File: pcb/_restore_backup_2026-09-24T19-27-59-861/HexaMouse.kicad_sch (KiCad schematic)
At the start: 23 parts, among them J1 Conn_01x02_Socket, J2 Conn_01x02_Socket, J3 Xiao_Headers_Left, J4 Xiao_Headers_Right, SW1 SW_SPDT, U2 TLV493D, U3 TLV493D, U4 TLV493D, U5 TCA9548APWR

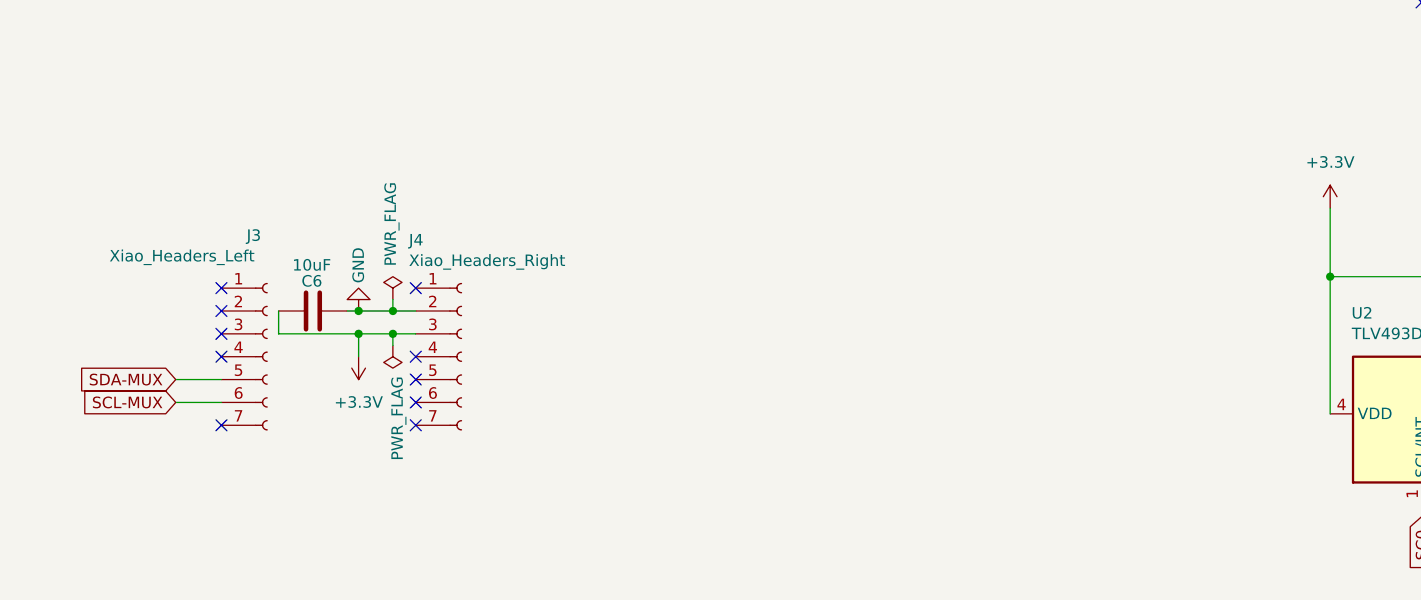
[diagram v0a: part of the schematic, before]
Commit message: Swapped from MCU to pins so i can use headers instead
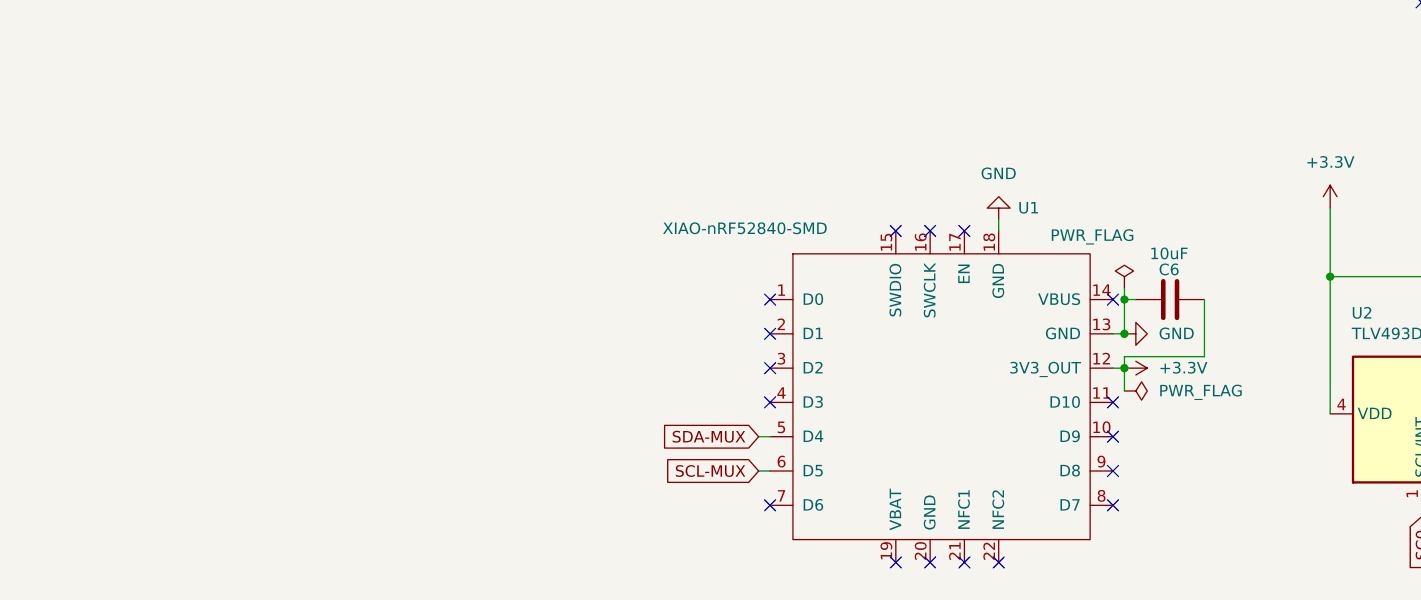
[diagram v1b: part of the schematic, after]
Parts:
- removed J3: Xiao_Headers_Left, symbol Connector:Conn_01x07_Socket
- removed J4: Xiao_Headers_Right, symbol Connector:Conn_01x07_Socket
- added U1: XIAO-nRF52840-SMD, Seeed_Studio_XIAO_Series:XIAO-nRF52840-SMD, symbol Seeed_Studio_XIAO_Series:XIAO-nRF52840-SMD
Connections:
- net +3.3V: now also C6.1, U1.12 (3V3_OUT); no longer C6.2
- net GND: now also C6.2, U1.13 (GND), U1.18 (GND); no longer C6.1
- net SCL-MUX: now also U1.6 (D5)
- net SDA-MUX: now also U1.5 (D4)
- no-connect marks 21 -> 28
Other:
- moved on the sheet: C6
